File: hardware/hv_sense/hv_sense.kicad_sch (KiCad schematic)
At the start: 25 parts, among them J1 Conn_01x02, J2 Conn_01x04, U1 TLV274, U2 TL431ACDT, U3 140817141410, U4 140817141410

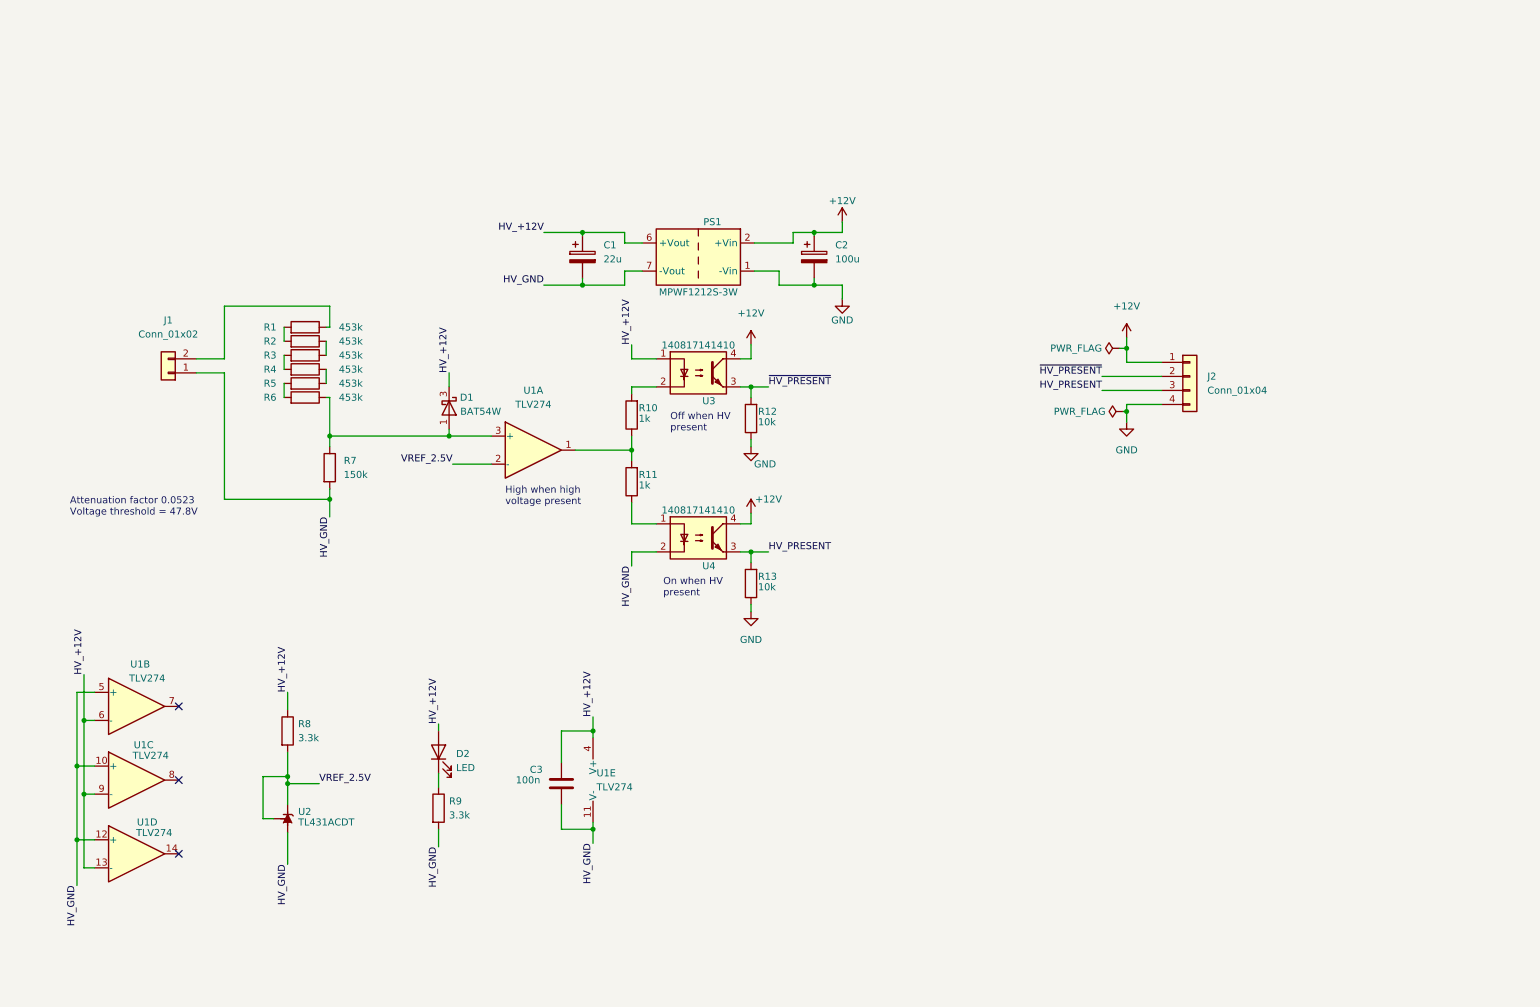
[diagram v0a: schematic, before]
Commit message: Integrated TSAL logic into hv_sense
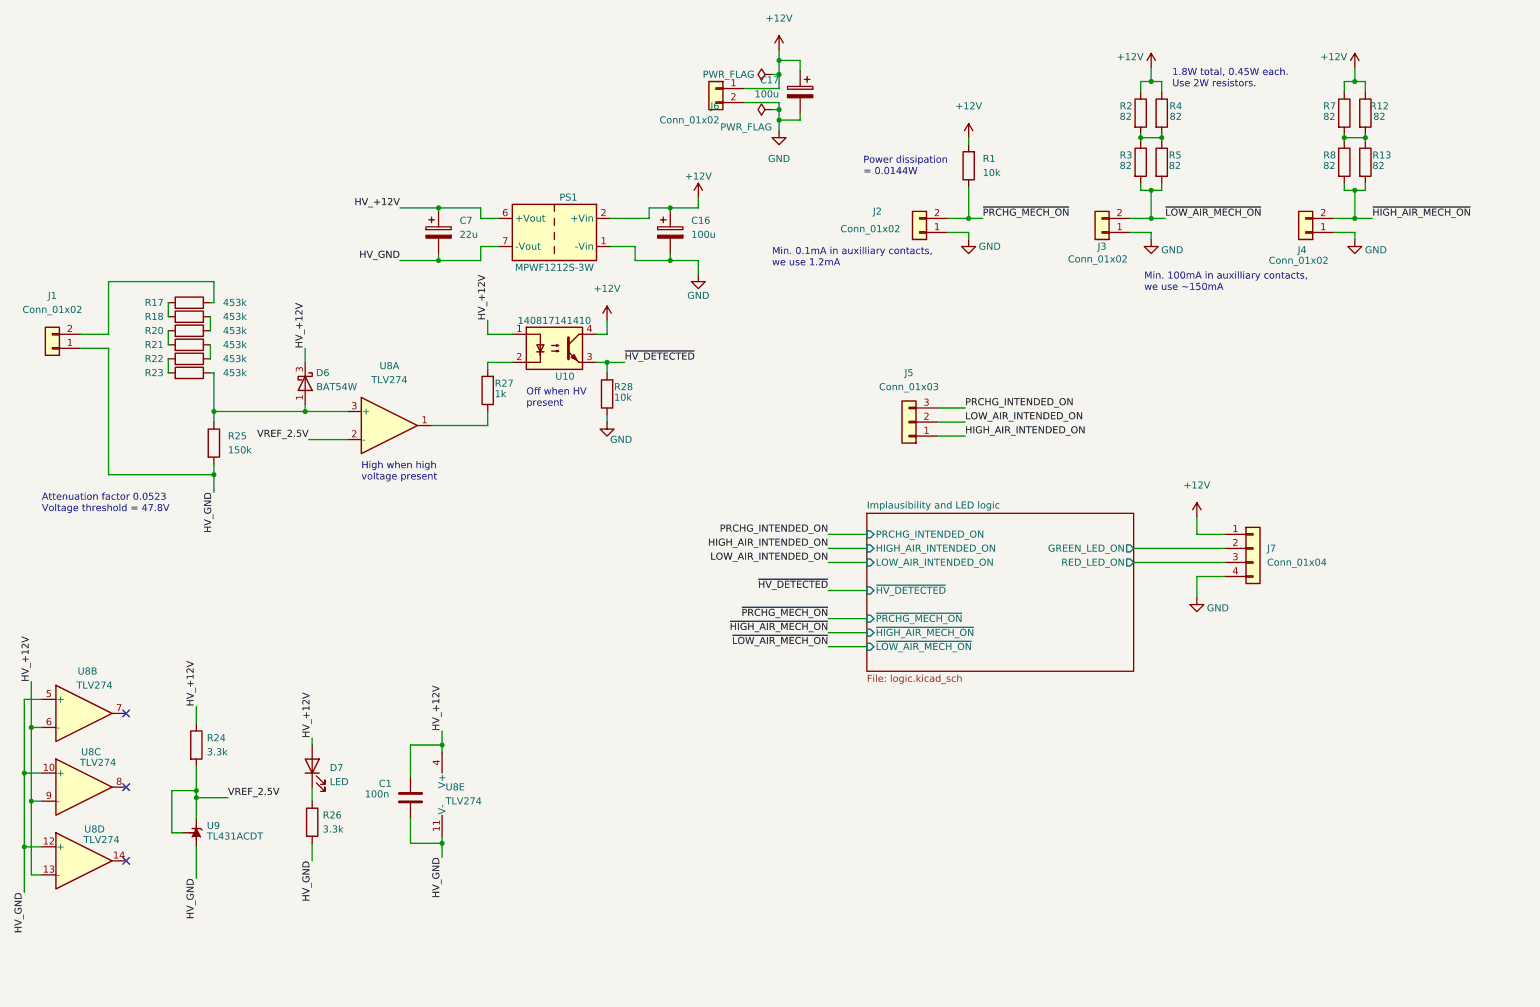
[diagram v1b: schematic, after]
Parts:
- removed J2: Conn_01x04, Connector_PinSocket_2.54mm:PinSocket_1x04_P2.54mm_Horizontal, symbol Connector_Generic:Conn_01x04
- removed R11: 1k, Resistor_SMD:R_1206_3216Metric, symbol Device:R
- removed U4: 140817141410, Package_DIP:DIP-4_W7.62mm, symbol Isolator:SFH617A-1
- added C17: 100u, Capacitor_THT:CP_Radial_D6.3mm_P2.50mm, symbol Device:C_Polarized
- added J2, J3, J4, J6: Conn_01x02, Connector_Molex:Molex_Micro-Fit_3.0_43650-0200_1x02_P3.00mm_Horizontal, symbol Connector_Generic:Conn_01x02
- added J5: Conn_01x03, Connector_Molex:Molex_Micro-Fit_3.0_43650-0300_1x03_P3.00mm_Horizontal, symbol Connector_Generic:Conn_01x03
- added J7: Conn_01x04, Connector_Molex:Molex_Micro-Fit_3.0_43650-0400_1x04_P3.00mm_Horizontal, symbol Connector_Generic:Conn_01x04
- added R1: 10k, Resistor_SMD:R_0603_1608Metric, symbol Device:R
- added R12, R2, R3, R4, R5, R7, R8: 82, Resistor_SMD:R_2512_6332Metric, symbol Device:R
- R13: value 10k -> 82; footprint Resistor_SMD:R_0603_1608Metric -> Resistor_SMD:R_2512_6332Metric
- renumbered C3 to C1, C2 to C16, C1 to C7, D1 to D6, D2 to D7, R1 to R17, R2 to R18, R3 to R20, R4 to R21, R5 to R22, R6 to R23, R8 to R24, R7 to R25, R9 to R26, R10 to R27, R12 to R28, U3 to U10, U1 to U8, U2 to U9
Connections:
- net +12V: now also C17.1, J6.1 (Pin_1), J7.1 (Pin_1), R1.2, R12.1, R2.1, R4.1, R7.1
- net GND: now also C17.2, J2.1 (Pin_1), J3.1 (Pin_1), J4.1 (Pin_1), J6.2 (Pin_2), J7.4 (Pin_4); no longer R13.1
- net HV_PRESENT renamed ~{HIGH_AIR_MECH_ON}
- net ~{HIGH_AIR_MECH_ON}: now also J4.2 (Pin_2), R8.2
- net ~{HV_PRESENT} renamed ~{HV_DETECTED}
- new net: R12.2, R13.1, R7.2, R8.1
- new net: R2.2, R3.1, R4.2, R5.1
- new net HIGH_AIR_INTENDED_ON: J5.1 (Pin_1)
- new net Implausibility and LED logic/GREEN_LED_ON: J7.2 (Pin_2)
- new net Implausibility and LED logic/RED_LED_ON: J7.3 (Pin_3)
- new net LOW_AIR_INTENDED_ON: J5.2 (Pin_2)
- new net PRCHG_INTENDED_ON: J5.3 (Pin_3)
- new net ~{LOW_AIR_MECH_ON}: J3.2 (Pin_2), R3.2, R5.2
- new net ~{PRCHG_MECH_ON}: J2.2 (Pin_2), R1.1
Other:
- added sheet Implausibility and LED logic (logic.kicad_sch)
- note added: "1.8W total, 0.45W each. Use 2W resistors."
- note added: "Min. 0.1mA in auxilliary contacts, we use 1.2mA"
- note added: "Min. 100mA in auxilliary contacts, we use ~150mA"
- note added: "Power dissipation = 0.0144W"
- note removed: "On when HV present"
- moved on the sheet: C1, C16, C7, D6, D7, J1, PS1, R17, R18, R20, R21, R22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

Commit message: Routing done, still needs finishing touches though
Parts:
- J1: footprint Connector_PinSocket_2.54mm:PinSocket_1x02_P2.54mm_Horizontal -> Connector_Molex:Molex_Micro-Fit_3.0_43650-0200_1x02_P3.00mm_Horizontal
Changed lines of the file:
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@@
     (property "Reference" "J1" (id 0) (at 24.765 66.675 0))
     (property "Value" "Conn_01x02" (id 1) (at 24.765 69.215 0))
-    (property "Footprint" "Connector_PinSocket_2.54mm:PinSocket_1x02_P2.54mm_Horizontal" (id 2) (at 24.765 76.2 0)
+    (property "Footprint" "Connector_Molex:Molex_Micro-Fit_3.0_43650-0200_1x02_P3.00mm_Horizontal" (id 2) (at 24.765 76.2 0)
       (effects (font (size 1.27 1.27)) hide)
     )
@@
     )
     (path "/6dc966bc-2ab4-485a-8775-1b6a82af49c3"
-      (reference "J1") (unit 1) (value "Conn_01x02") (footprint "Connector_PinSocket_2.54mm:PinSocket_1x02_P2.54mm_Horizontal")
+      (reference "J1") (unit 1) (value "Conn_01x02") (footprint "Connector_Molex:Molex_Micro-Fit_3.0_43650-0200_1x02_P3.00mm_Horizontal")
     )
     (path "/8b5ef870-c787-47b8-8a14-ed9256c6b5f1"

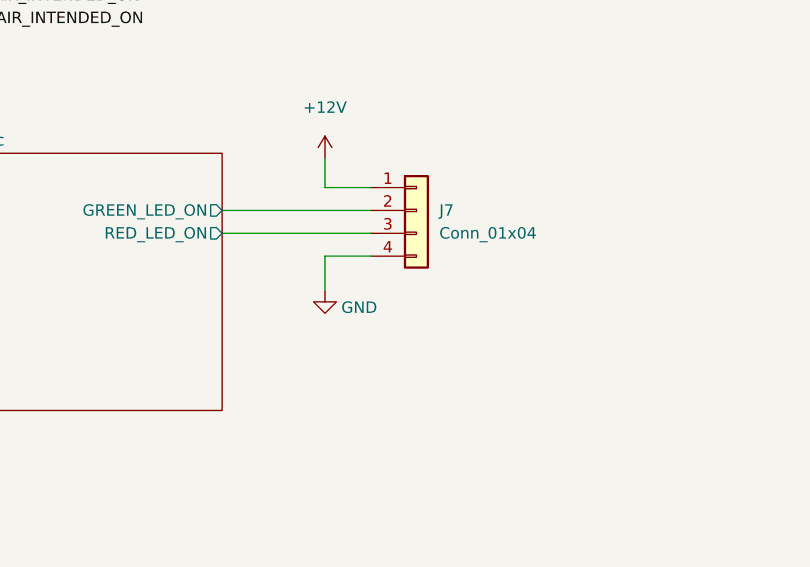
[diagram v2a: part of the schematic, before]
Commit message: Added edge, moved component references to be visible
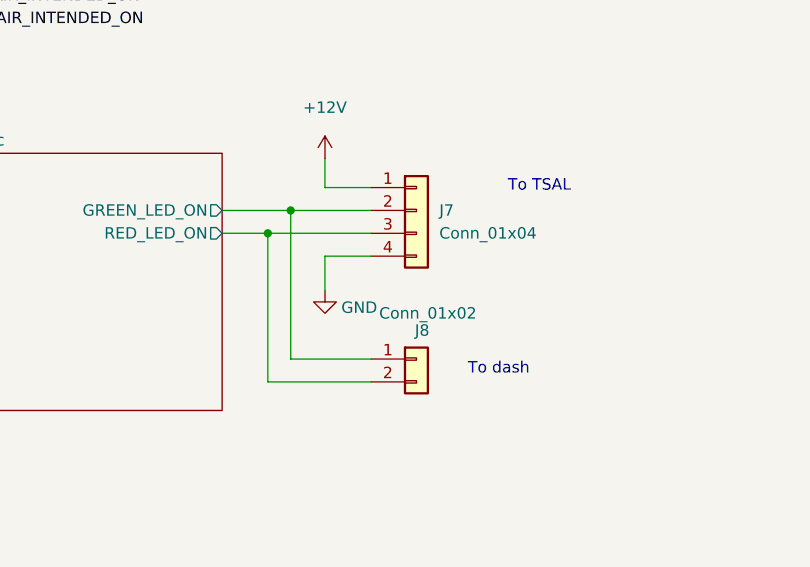
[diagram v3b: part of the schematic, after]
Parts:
- added J8: Conn_01x02, Connector_Molex:Molex_Micro-Fit_3.0_43650-0200_1x02_P3.00mm_Horizontal, symbol Connector_Generic:Conn_01x02
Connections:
- net Implausibility and LED logic/GREEN_LED_ON: now also J8.1 (Pin_1)
- net Implausibility and LED logic/RED_LED_ON: now also J8.2 (Pin_2)
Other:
- note added: "To TSAL"
- note added: "To dash"
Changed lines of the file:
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@@
   (junction (at 70.485 87.63) (diameter 0) (color 0 0 0 0)
+  )
+  (junction (at 227.965 112.395) (diameter 0) (color 0 0 0 0)
+  )
+  (junction (at 225.425 114.935) (diameter 0) (color 0 0 0 0)
   )
   (junction (at 156.21 26.67) (diameter 0) (color 0 0 0 0)
@@
     (stroke (width 0) (type default) (color 0 0 0 0))
   )
+  (wire (pts (xy 227.965 112.395) (xy 236.855 112.395))
+    (stroke (width 0) (type default) (color 0 0 0 0))
+  )
   (wire (pts (xy 107.95 73.66) (xy 103.505 73.66))
     (stroke (width 0) (type default) (color 0 0 0 0))
@@
     (stroke (width 0) (type default) (color 0 0 0 0))
   )
+  (wire (pts (xy 236.855 131.445) (xy 225.425 131.445))
+    (stroke (width 0) (type default) (color 0 0 0 0))
+  )
   (wire (pts (xy 103.505 78.74) (xy 103.505 80.01))
     (stroke (width 0) (type default) (color 0 0 0 0))
@@
     (stroke (width 0) (type default) (color 0 0 0 0))
   )
-  (wire (pts (xy 220.345 112.395) (xy 236.855 112.395))
+  (wire (pts (xy 220.345 112.395) (xy 227.965 112.395))
     (stroke (width 0) (type default) (color 0 0 0 0))
   )
@@
     (stroke (width 0) (type default) (color 0 0 0 0))
   )
-  (wire (pts (xy 220.345 114.935) (xy 236.855 114.935))
+  (wire (pts (xy 236.855 128.905) (xy 227.965 128.905))
+    (stroke (width 0) (type default) (color 0 0 0 0))
+  )
+  (wire (pts (xy 220.345 114.935) (xy 225.425 114.935))
     (stroke (width 0) (type default) (color 0 0 0 0))
   )
@@
     (stroke (width 0) (type default) (color 0 0 0 0))
   )
+  (wire (pts (xy 225.425 131.445) (xy 225.425 114.935))
+    (stroke (width 0) (type default) (color 0 0 0 0))
+  )
   (wire (pts (xy 260.35 25.4) (xy 260.35 27.94))
     (stroke (width 0) (type default) (color 0 0 0 0))
@@
     (stroke (width 0) (type default) (color 0 0 0 0))
   )
+  (wire (pts (xy 227.965 128.905) (xy 227.965 112.395))
+    (stroke (width 0) (type default) (color 0 0 0 0))
+  )
   (wire (pts (xy 103.505 71.12) (xy 103.505 73.66))
     (stroke (width 0) (type default) (color 0 0 0 0))
@@
     (stroke (width 0) (type default) (color 0 0 0 0))
   )
+  (wire (pts (xy 225.425 114.935) (xy 236.855 114.935))
+    (stroke (width 0) (type default) (color 0 0 0 0))
+  )
   (wire (pts (xy 160.02 24.13) (xy 156.21 24.13))
     (stroke (width 0) (type default) (color 0 0 0 0))
@@
   )
   (text "Min. 0.1mA in auxilliary contacts,\nwe use 1.2mA" (at 154.94 61.595 0)
+    (effects (font (size 1.27 1.27)) (justify left bottom))
+  )
+  (text "To TSAL" (at 252.095 110.49 0)
     (effects (font (size 1.27 1.27)) (justify left bottom))
   )
@@
   )
   (text "Min. 100mA in auxilliary contacts,\nwe use ~150mA" (at 222.25 66.04 0)
+    (effects (font (size 1.27 1.27)) (justify left bottom))
+  )
+  (text "To dash" (at 247.65 130.81 0)
     (effects (font (size 1.27 1.27)) (justify left bottom))
   )
@@
     (pin "2")
   )
+  (symbol (lib_id "Connector_Generic:Conn_01x02") (at 241.935 128.905 0) (unit 1)
+    (in_bom yes) (on_board yes)
+    (property "Reference" "J8" (id 0) (at 242.57 125.73 0))
+    (property "Value" "Conn_01x02" (id 1) (at 243.205 123.825 0))
+    (property "Footprint" "Connector_Molex:Molex_Micro-Fit_3.0_43650-0200_1x02_P3.00mm_Horizontal" (id 2) (at 241.935 128.905 0)
+      (effects (font (size 1.27 1.27)) hide)
+    )
+    (property "Datasheet" "~" (id 3) (at 241.935 128.905 0)
+      (effects (font (size 1.27 1.27)) hide)
+    )
+    (pin "1")
+    (pin "2")
+  )
   (symbol (lib_id "Device:R") (at 225.425 33.655 0) (unit 1)
     (in_bom yes) (on_board yes)
@@
       (reference "J7") (unit 1) (value "Conn_01x04") (footprint "Connector_Molex:Molex_Micro-Fit_3.0_43650-0400_1x04_P3.00mm_Horizontal")
     )
+    (path "/8104aa50-a939-4715-a570-a261cb482238"
+      (reference "J8") (unit 1) (value "Conn_01x02") (footprint "Connector_Molex:Molex_Micro-Fit_3.0_43650-0200_1x02_P3.00mm_Horizontal")
+    )
     (path "/f345e52a-8e0a-425a-b438-90809dd3b799"

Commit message: ??
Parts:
- added R?: 105k, symbol Device:R
- R23: value 453k -> 348k
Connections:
- net at D6.1 (A), R23.1: now also R?.1; no longer R25.1, U8.3 (+)
- new net: R25.1, R?.2, U8.3 (+)
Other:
- note added: "For low input voltages, the diode is reverse biased and there is an attenuation ratio of 0.0523, giving a voltage threshold of 47.8V. Diode D6 clamps the voltage to 7.06V, to prevent damage to the op-amp."
- note removed: "Attenuation factor 0.0523 Voltage threshold = 47.8V"
- moved on the sheet: D6, R17, R18, R20, R21, R22, R23

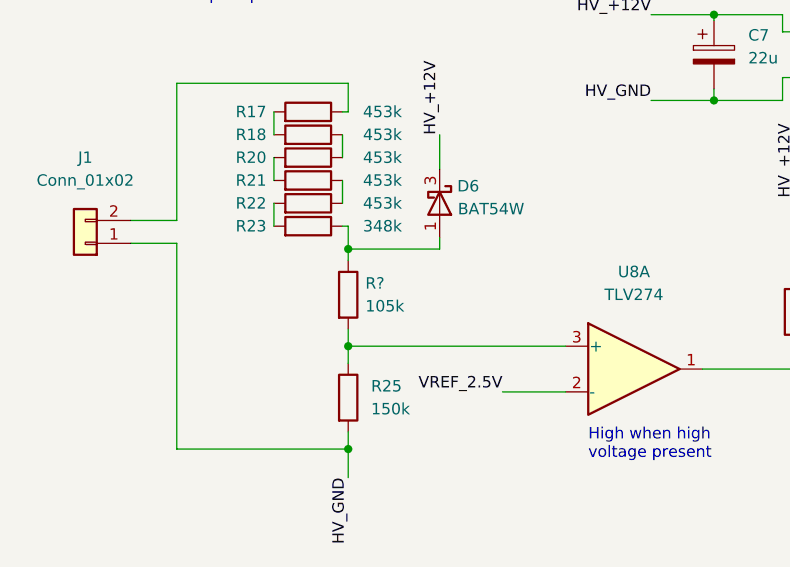
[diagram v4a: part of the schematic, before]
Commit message: Capped voltage input to opamp
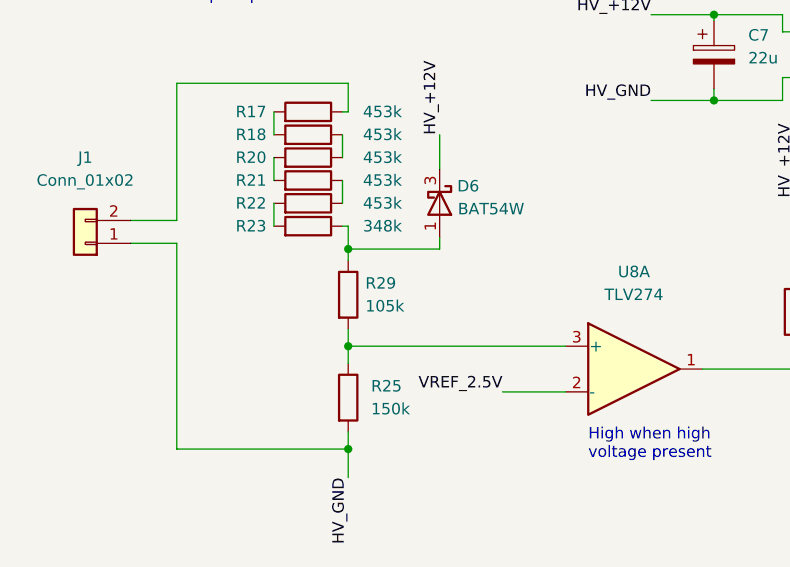
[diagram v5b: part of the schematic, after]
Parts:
- R29: renamed from R?; footprint (none) -> Resistor_SMD:R_0805_2012Metric
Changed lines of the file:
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@@
   (symbol (lib_id "Device:R") (at 53.975 81.915 0) (unit 1)
     (in_bom yes) (on_board yes) (fields_autoplaced)
-    (property "Reference" "R?" (id 0) (at 55.88 80.6449 0)
+    (property "Reference" "R29" (id 0) (at 55.88 80.6449 0)
       (effects (font (size 1.27 1.27)) (justify left))
     )
@@
       (effects (font (size 1.27 1.27)) (justify left))
     )
-    (property "Footprint" "" (id 2) (at 52.197 81.915 90)
+    (property "Footprint" "Resistor_SMD:R_0805_2012Metric" (id 2) (at 52.197 81.915 90)
       (effects (font (size 1.27 1.27)) hide)
     )
@@
     )
     (path "/2d8e17b7-380e-447b-84c1-91132b7c52b6"
-      (reference "R?") (unit 1) (value "105k") (footprint "")
+      (reference "R29") (unit 1) (value "105k") (footprint "Resistor_SMD:R_0805_2012Metric")
     )
     (path "/500b8546-e16a-470a-a6c0-6857508d9ee2/0f9aa347-2c25-4973-8b7b-3c2ce535e77c"
